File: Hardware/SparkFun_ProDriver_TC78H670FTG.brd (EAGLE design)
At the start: 50.8 x 57.1 mm, 127 parts, among them J2 LATCH, J3 PTH, J4 LATCH, J5 LATCH, J6 PTH, J7 LATCH, J8 PTH, U1 TC78H670FTG, U2 LM1117

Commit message: rotated GND/VM bottom labels to read same direction as others
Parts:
- moved U$73 0.25 mm to (41.9, 2.69), turned to 270 degrees
- turned U$72 to 270 degrees
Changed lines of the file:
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@@
 <element name="U$69" library="output" package="#GND#0" value="" x="46.370240625" y="8.82141875" smashed="yes" rot="MR0"/>
 <element name="U$70" library="output" package="#GND#5" value="" x="14.0081" y="52.664359375" smashed="yes" rot="MR270"/>
-<element name="U$72" library="output" package="#VM#0" value="" x="36.878265625" y="2.93624375" smashed="yes" rot="MR90"/>
-<element name="U$73" library="output" package="#GND#0" value="" x="41.856659375" y="2.94131875" smashed="yes" rot="MR90"/>
+<element name="U$72" library="output" package="#VM#0" value="" x="36.88079375" y="2.98195625" smashed="yes" rot="MR270"/>
+<element name="U$73" library="output" package="#GND#0" value="" x="41.861740625" y="2.694940625" smashed="yes" rot="MR270"/>
 <element name="U$74" library="output" package="#STBY#1" value="" x="16.537940625" y="55.5371" smashed="yes" rot="MR270"/>
 <element name="U$71" library="output" package="#ERR#3" value="" x="19.077940625" y="55.5371" smashed="yes" rot="MR270"/>

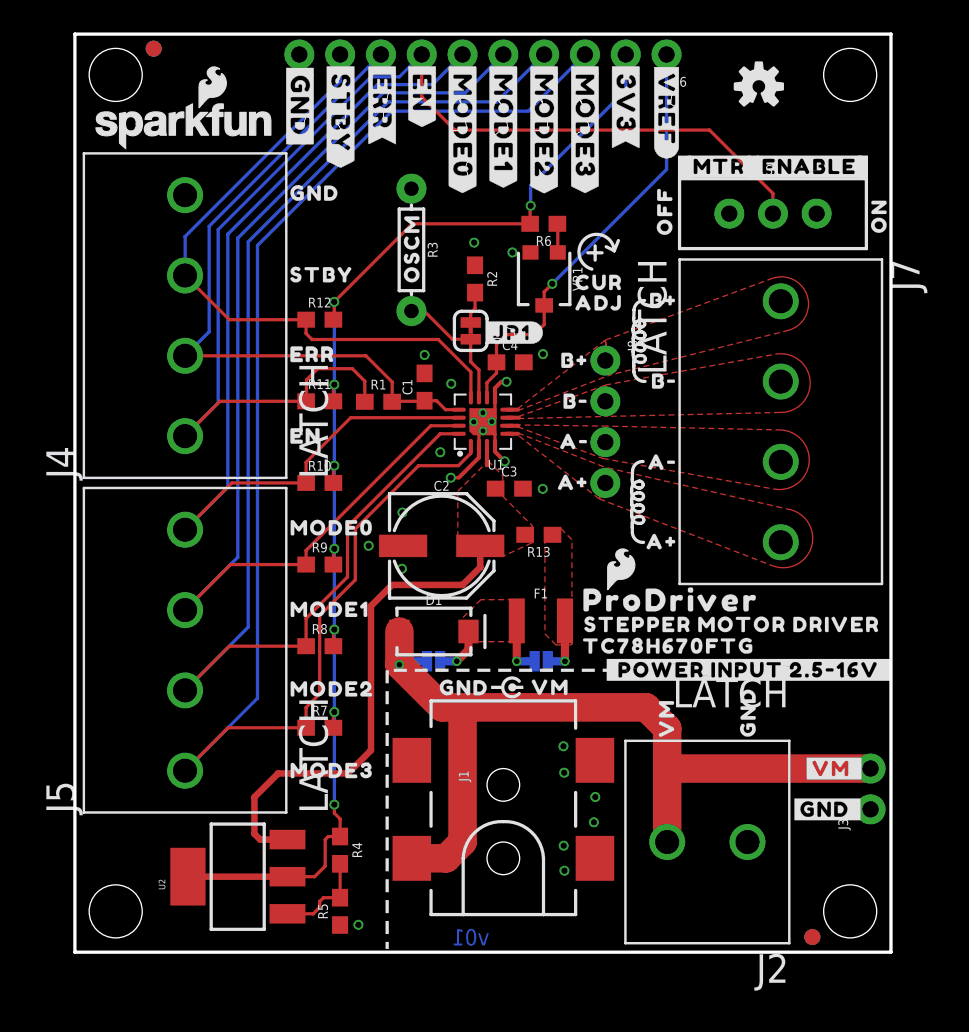
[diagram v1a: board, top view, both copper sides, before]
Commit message: first run of checklist catches (pre-design review)
-4-layer board warnings in sch, brd, plus 1,2,3,4 in coppers
-added power LED
-added specail ordering instructions for 4-layer and 2 oz copper
-added measures
-ERR and STBY labels show active low overline now
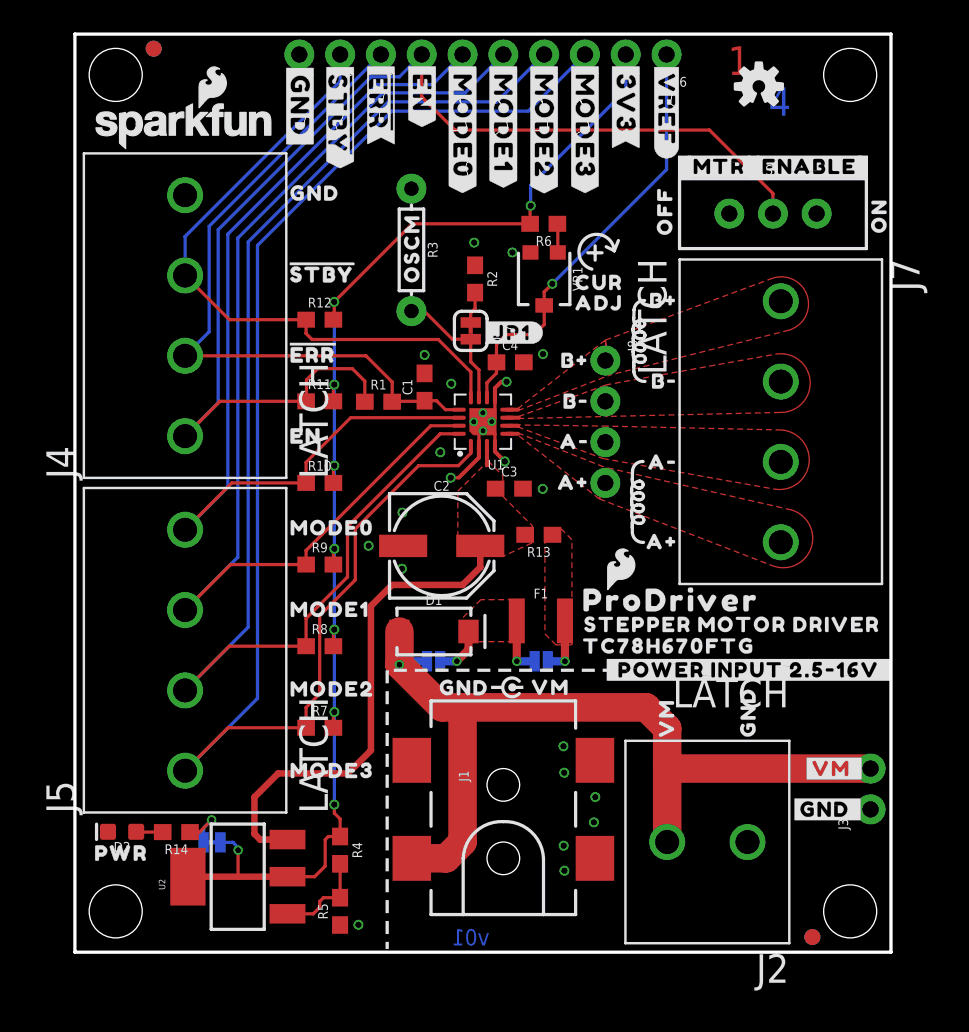
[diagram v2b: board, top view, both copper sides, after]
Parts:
- removed U$7: (no value), output:#ERR#7
- removed U$71: (no value), output:#ERR#3
- removed U$74: (no value), output:#STBY#1
- added D2: RED, SparkFun-LED:LED-0603
- added JP4: LED, SparkFun-Jumpers:SMT-JUMPER_2_NC_TRACE_SILK
- added LOGO3: SPECIAL_INSTRUCTIONS-ORDERING, SparkFun-Aesthetics:ORDERING_INSTRUCTIONS
- added LOGO5: SFE_LOGO_NAME_FLAME.1_INCH, SparkFun-Aesthetics:SFE_LOGO_NAME_FLAME_.1
- added R14: 1k, SparkFun-Resistors:0603
- added U$39: (no value), output:#LED#0
- added U$83: (no value), output:PWR0
- added U$84: (no value), output:TC78H670FTG0
- added U$85: (no value), output:STEPPER_MOTOR_DRIVER0
- added U$86: (no value), output:PRODRIVER0
- added U$87: (no value), output:##STBY##0
- added U$88: (no value), output:##STBY##1
- added U$89: (no value), output:#STBY#2
- U$34: device output:#STBY#3 -> output:##ERR##5
- U$36: device output:ERR4 -> output:##ERR##6
- U$53: device output:#STBY#0 -> output:##STBY##1
- U$54: device output:#ERR#0 -> output:##ERR##6
- U$8: device output:STBY8 -> output:#ERR#3
- moved U$54 24.6 mm to (19.1, 55.5), turned to 270 degrees
- moved U$34 21.5 mm to (5.62, 37.0), flipped to the bottom, turned to 0 degrees
- moved U$36 19.4 mm to (19.1, 55.5), turned to 270 degrees
- moved U$53 19.1 mm to (16.5, 55.5), flipped to the top, turned to 270 degrees
- moved U$8 4.85 mm to (12.7, 37.3)
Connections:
- new net N$6: D2.A, R14.2
- new net N$8: JP4.1, R14.1
- net 3.3V: now also JP4.2
- net GND: now also D2.C
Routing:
- net N$8: track 0.00 -> 3.27 mm, vias 0 -> 1
- net 3.3V: track 78.5 -> 81.5 mm, vias 8 -> 9
- net N$6: track 0.00 -> 1.66 mm
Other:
- board text added: "1"
- board text added: "2"
- board text added: "3"
- board text added: "4"
- board text added: "4-Layer Board 2 OZ Copper"
- board text added: "LAYER NUMBERS"
- board text added: "Selective Solder Nozzle Width: 0.354""
- board text added: "This is a 4-LAYER board!"

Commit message: ERR and STBY NET names to active low - now with overline
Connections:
- net ERR renamed !ERR
- net STBY renamed !STBY
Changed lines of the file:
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@@
 <wire x1="23.50008125" y1="38.155878125" x2="21.747478125" y2="39.90848125" width="0.2032" layer="1"/>
 </signal>
-<signal name="STBY">
+<signal name="!STBY">
 <contactref element="U1" pad="12"/>
 <contactref element="R12" pad="1"/>
@@
 <wire x1="6.858" y1="32.124" x2="9.024" y2="34.29" width="0.2032" layer="1"/>
 </signal>
-<signal name="ERR">
+<signal name="!ERR">
 <contactref element="U1" pad="13"/>
 <contactref element="R1" pad="2"/>

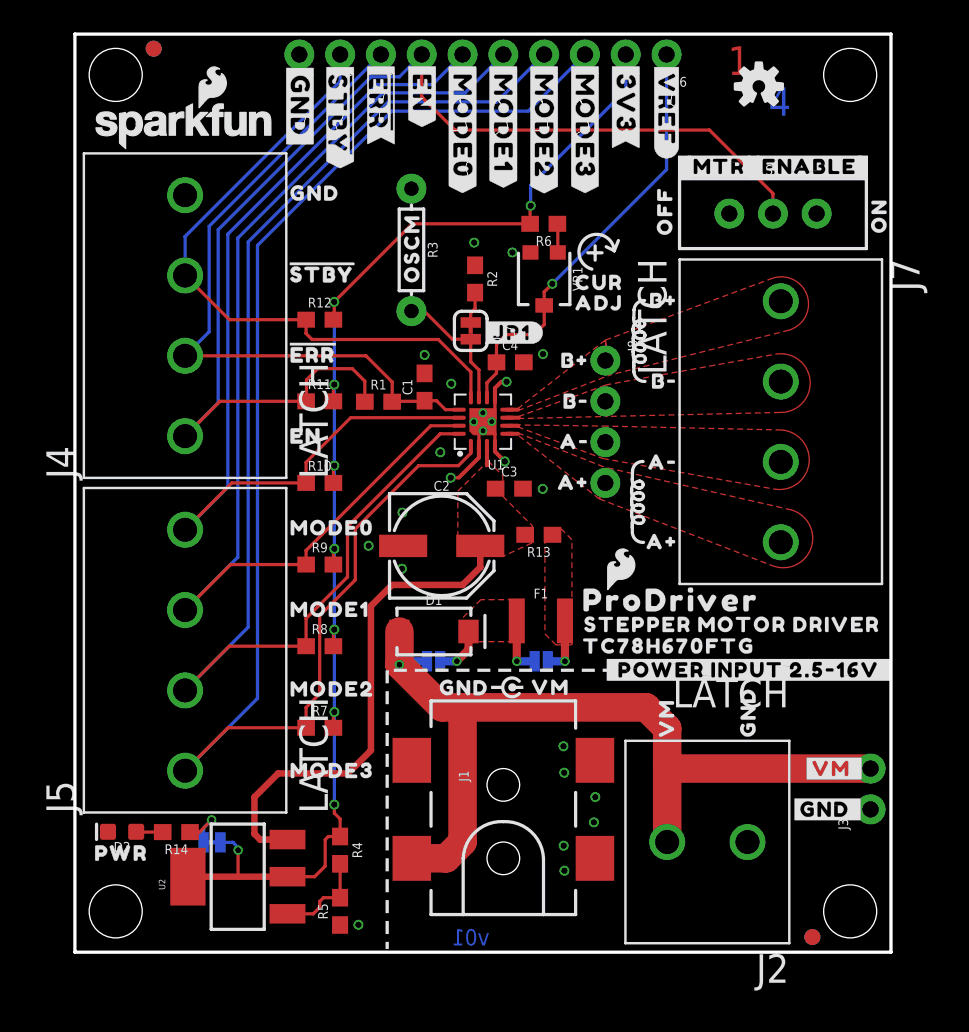
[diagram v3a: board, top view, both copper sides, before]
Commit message: Moved to pull-downs on EN and STBY
Because the powerup sequence requires that EN and STBY be low (while VM comes up), we should default these to low. Then the user can wire up these lines to their micro and write them HIGH when necessary.
-Adjusted how the enable hardware slide switch works. Now it simply disconnects the "user" control, so that it lets the pull-down resistor take effect. In this way, it will overide any logic level the user has provided on EN.
-Changes enable switch silk label to "user" indicating that the user must now provide logic control on the latch terminals or PTH headers.
-Added note in schematic about logic level tolerances
-re routed and moves some traces to maintain better top copper flow.
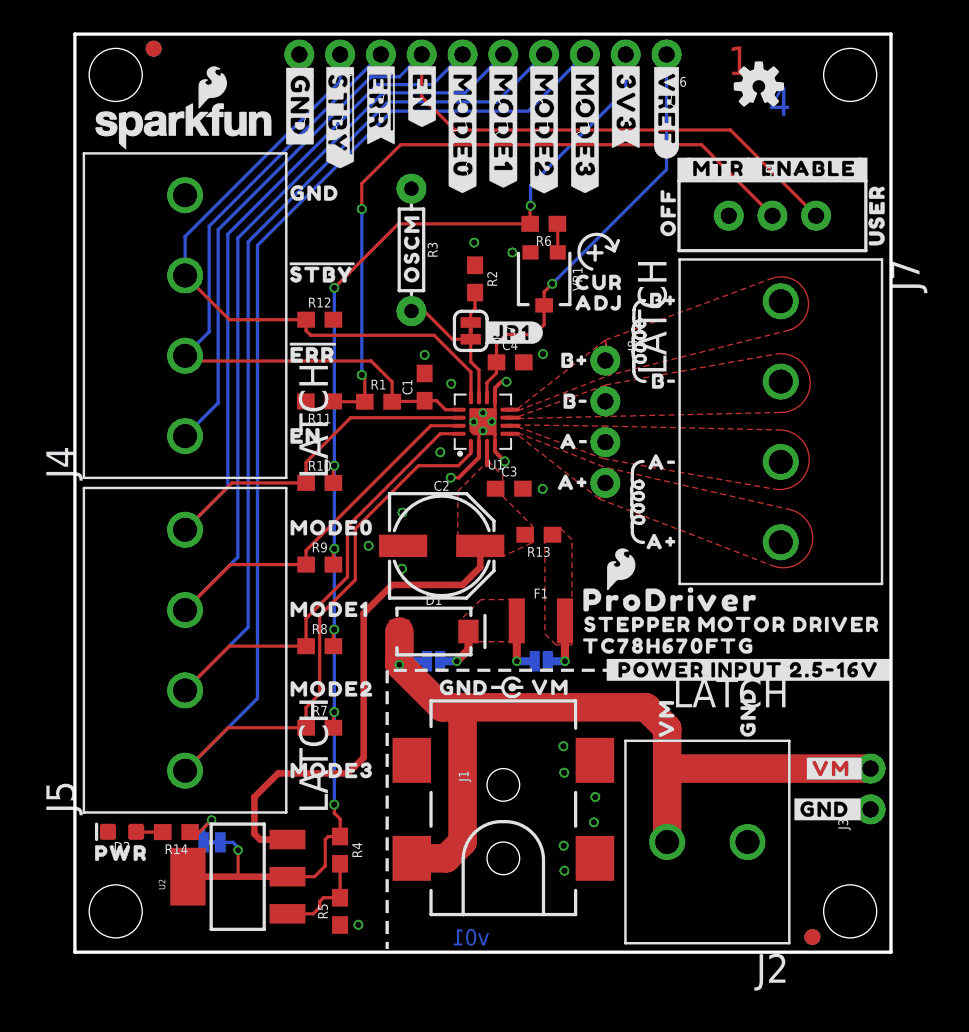
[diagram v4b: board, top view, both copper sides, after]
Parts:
- removed U$16: (no value), output:ON0
- added U$7: (no value), output:USER0
- moved U$17 0.23 mm to (36.9, 43.9)
- moved S1 0.13 mm to (43.4, 45.8)
- moved U$14 0.13 mm to (37.8, 48.8)
- moved U$21 0.13 mm to (42.0, 48.8)
- turned R11 to 180 degrees
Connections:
- new net N$7: R1.1, R11.1, S1.2
- net 3.3V: no longer R11.2, R12.2
- net EN: now also S1.1; no longer R1.1, R11.1, S1.2
- net GND: now also R11.2, R12.2; no longer S1.3
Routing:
- net N$7: track 0.00 -> 44.0 mm, vias 0 -> 2
- net EN: track 74.5 -> 61.1 mm
- net 3.3V: track 81.5 -> 79.8 mm, vias 9 -> 8
